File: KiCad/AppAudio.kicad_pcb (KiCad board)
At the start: 2 copper layers, 4.3 x 3.1 mm, 32 parts, among them P1 WRITER-VCC, Q1 Q_NMOS_SGD, SW1 SWITCH_INV, SW2 SW_PUSH, U1 TWE_LITE_SMD, U2 LMC6062, U3 HT82V739

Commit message: PCB design in progress.
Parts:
- added REF**: PCB-LC115H, favorites:PCB-LC115H, F.Cu at (100.0, 100.0)
- R10, R13, R4: footprint Resistors_ThroughHole:Resistor_Horizontal_RM10mm -> Resistors_SMD:R_0603_HandSoldering
- SW1: value SWITCH_INV -> SW_PUSH; footprint Terminal_Blocks:TerminalBlock_WAGO-236_2Stift_RM5mm_3pol -> favorites:JB-15HFBP2
- SW2: footprint favorites:JB-15HFBP2 -> favorites:DTS-6
- VR1, VR2: footprint favorites:RV-TSR-3386T -> favorites:RV-3362P
- moved R9 123.8 mm to (1.84, 133.5)
- moved P1 122.7 mm to (73.5, 94.0), turned to 270 degrees
- moved SP1 116.6 mm to (3.41, 162.3)
- moved C2 116.6 mm to (-22.8, 100.3)
- moved C4 116.6 mm to (-18.5, 102.1)
- moved C5 116.6 mm to (-31.3, 105.7)
- moved Q1 116.6 mm to (-7.20, 125.5)
- moved R11 116.6 mm to (37.4, 126.8)
- moved C7 116.6 mm to (-27.0, 107.4)
- moved R12 116.6 mm to (50.2, 125.0)
- moved R7 116.6 mm to (10.3, 149.2)
- moved R8 116.6 mm to (10.1, 143.2)
- moved R4 94.4 mm to (148.0, 92.5), turned to 0 degrees
- moved R13 91.8 mm to (87.0, 52.5)
- moved R10 87.8 mm to (50.0, 64.0)
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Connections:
- SW1 pad 1: GND -> Net-(SW1-Pad1)
- SW1 pad 2: Net-(SW1-Pad2) -> GND
- U1 pad 13: Net-(SW2-Pad1) -> Net-(SW1-Pad1)
- U1 pad 15: Net-(SW1-Pad2) -> Net-(SW2-Pad1)
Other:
- board size 4.3 x 3.1 mm -> 60 x 63 mm

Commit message: Fixed wires.
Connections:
- U1 pad 8: /RXD -> /TXD
- U1 pad 9: /TXD -> /RXD
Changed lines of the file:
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@@
     (links 67)
     (no_connects 67)
-    (area -32.687973 49.475 150.225001 181.591001)
+    (area 0 0 0 0)
     (thickness 1.6)
     (drawings 0)
@@
       (net 35 "Net-(U1-Pad7)"))
     (pad 8 smd oval (at -6.735 4.445 90) (size 0.9 1.4) (layers F.Cu F.Paste F.Mask)
+      (net 18 /TXD))
+    (pad 9 smd oval (at -4.445 6.735) (size 0.9 1.4) (layers F.Cu F.Paste F.Mask)
       (net 16 /RXD))
-    (pad 9 smd oval (at -4.445 6.735) (size 0.9 1.4) (layers F.Cu F.Paste F.Mask)
-      (net 18 /TXD))
     (pad 10 smd oval (at -3.175 6.735) (size 0.9 1.4) (layers F.Cu F.Paste F.Mask)
       (net 36 "Net-(U1-Pad10)"))

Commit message: PCB layout has done.
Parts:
- added BT1: Battery, Pin_Headers:Pin_Header_Straight_1x02, B.Cu at (110.5, 124.0)
- C1, C3, P1, Q1, R10, R13, R4, SP1, VR1, VR2: moved to B.Cu
- C6: footprint Capacitors_ThroughHole:C_Radial_D8_L11.5_P3.5 -> Capacitors_ThroughHole:C_Radial_D6.3_L11.2_P2.5; moved to B.Cu
- MIC1: footprint Capacitors_ThroughHole:C_Radial_D6.3_L11.2_P2.5 -> favorites:DB-C9767
- moved C5 151.9 mm to (118.0, 77.5), turned to 180 degrees
- moved C4 137.8 mm to (119.0, 94.0), turned to 270 degrees
- moved C2 137.4 mm to (114.5, 94.0), turned to 270 degrees
- moved R7 121.7 mm to (122.5, 102.0), turned to 270 degrees
- moved R8 114.5 mm to (117.0, 102.0), turned to 270 degrees
- moved C7 113.6 mm to (86.5, 111.5), turned to 180 degrees
- moved SP1 112.1 mm to (75.5, 76.5), turned to 180 degrees
- moved R9 104.9 mm to (100.3, 97.5)
- moved Q1 103.7 mm to (85.0, 78.0)
- moved R5 78.9 mm to (107.5, 102.0), turned to 270 degrees
- moved C3 77.6 mm to (113.5, 117.0)
- moved R6 72.4 mm to (77.5, 112.2)
- moved R3 70.6 mm to (123.5, 98.0)
- moved VR1 70.5 mm to (114.0, 71.5), turned to 180 degrees
- moved R2 64.1 mm to (112.5, 102.0), turned to 270 degrees
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
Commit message: Relocated.
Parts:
- moved C6 13.0 mm to (93.0, 112.0)
- moved R10 10.6 mm to (77.0, 88.0)
- moved Q1 10.4 mm to (82.0, 88.0)
- moved R13 10.4 mm to (86.5, 88.1)
- moved C1 5.15 mm to (72.0, 110.0), turned to 0 degrees
- moved VR2 2.51 mm to (77.0, 120.0)
- moved SP1 2.20 mm to (77.5, 77.5), turned to 270 degrees
- moved R6 0.50 mm to (78.0, 112.2)
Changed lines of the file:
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@@
   )
   (module Resistors_ThroughHole:Resistor_Horizontal_RM10mm (layer F.Cu)
-    (at 77.5 112.16 90)
+    (at 78 112.16 90)
     (descr "Resistor, Axial,  RM 10mm, 1/3W")
     (tags "Resistor Axial RM 10mm 1/3W")
@@
   )
   (module Capacitors_ThroughHole:C_Radial_D8_L11.5_P3.5 (layer B.Cu)
-    (at 74.5 105.5 270)
+    (at 72 110)
     (descr "Radial Electrolytic Capacitor Diameter 8mm x Length 11.5mm, Pitch 3.5mm")
     (tags "Electrolytic Capacitor")
-    (fp_text reference C1 (at 1.75 5.3 270) (layer B.SilkS)
-      (effects (font (size 1 1) (thickness 0.15)) (justify mirror))
-    )
-    (fp_text value 33u (at 1.75 -5.3 270) (layer B.Fab)
+    (fp_text reference C1 (at 1.75 5.3) (layer B.SilkS)
+      (effects (font (size 1 1) (thickness 0.15)) (justify mirror))
+    )
+    (fp_text value 33u (at 1.75 -5.3) (layer B.Fab)
       (effects (font (size 1 1) (thickness 0.15)) (justify mirror))
     )
@@
     (fp_circle (center 1.75 0) (end 1.75 4.0375) (layer B.SilkS) (width 0.15))
     (fp_circle (center 1.75 0) (end 1.75 4.3) (layer B.CrtYd) (width 0.05))
-    (pad 2 thru_hole circle (at 3.5 0 270) (size 1.3 1.3) (drill 0.8) (layers *.Cu *.Mask B.SilkS)
+    (pad 2 thru_hole circle (at 3.5 0) (size 1.3 1.3) (drill 0.8) (layers *.Cu *.Mask B.SilkS)
       (net 2 "Net-(C1-Pad2)"))
-    (pad 1 thru_hole rect (at 0 0 270) (size 1.3 1.3) (drill 0.8) (layers *.Cu *.Mask B.SilkS)
+    (pad 1 thru_hole rect (at 0 0) (size 1.3 1.3) (drill 0.8) (layers *.Cu *.Mask B.SilkS)
       (net 1 "Net-(C1-Pad1)"))
     (model Capacitors_ThroughHole.3dshapes/C_Radial_D8_L11.5_P3.5.wrl
@@
   )
   (module favorites:EMT3 (layer B.Cu)
-    (at 85 78)
+    (at 82 88)
     (descr EMT3)
     (attr smd)
-    (fp_text reference Q1 (at 0 -1.524) (layer B.SilkS)
-      (effects (font (size 0.29972 0.29972) (thickness 0.06096)) (justify mirror))
+    (fp_text reference Q1 (at 0 -2.5) (layer B.SilkS)
+      (effects (font (size 1 1) (thickness 0.1)) (justify mirror))
     )
     (fp_text value Q_NMOS_SGD (at 0 -0.3302) (layer B.SilkS) hide
@@
   )
   (module Pin_Headers:Pin_Header_Straight_1x02 (layer B.Cu)
-    (at 75.5 76.5 180)
+    (at 77.46 77.5 270)
     (descr "Through hole pin header")
     (tags "pin header")
-    (fp_text reference SP1 (at 0 5.1 180) (layer B.SilkS)
-      (effects (font (size 1 1) (thickness 0.15)) (justify mirror))
-    )
-    (fp_text value SPEAKER (at 0 3.1 180) (layer B.Fab)
+    (fp_text reference SP1 (at 0 2.46 270) (layer B.SilkS)
+      (effects (font (size 1 1) (thickness 0.15)) (justify mirror))
+    )
+    (fp_text value SPEAKER (at 0.5 -5.54 270) (layer B.Fab)
       (effects (font (size 1 1) (thickness 0.15)) (justify mirror))
     )
@@
     (fp_line (start -1.27 -1.27) (end -1.27 -3.81) (layer B.SilkS) (width 0.15))
     (fp_line (start -1.27 -3.81) (end 1.27 -3.81) (layer B.SilkS) (width 0.15))
-    (pad 1 thru_hole rect (at 0 0 180) (size 2.032 2.032) (drill 1.016) (layers *.Cu *.Mask B.SilkS)
+    (pad 1 thru_hole rect (at 0 0 270) (size 2.032 2.032) (drill 1.016) (layers *.Cu *.Mask B.SilkS)
       (net 27 "Net-(SP1-Pad1)"))
-    (pad 2 thru_hole oval (at 0 -2.54 180) (size 2.032 2.032) (drill 1.016) (layers *.Cu *.Mask B.SilkS)
+    (pad 2 thru_hole oval (at 0 -2.54 270) (size 2.032 2.032) (drill 1.016) (layers *.Cu *.Mask B.SilkS)
       (net 28 "Net-(SP1-Pad2)"))
     (model Pin_Headers.3dshapes/Pin_Header_Straight_1x02.wrl
@@
   (module favorites:PCB-LC115H (layer F.Cu)
     (at 96.5 98.5)
-    (fp_text reference REF** (at 0 26) (layer F.SilkS)
+    (fp_text reference REF** (at -0.5 -33.5) (layer F.SilkS)
       (effects (font (size 1 1) (thickness 0.15)))
     )
@@
       (effects (font (size 1 1) (thickness 0.15)))
     )
-    (fp_text value SW_PUSH (at 0 -6.6 90) (layer F.SilkS)
+    (fp_text value SW_PUSH (at 0 -6.6 90) (layer F.Fab)
       (effects (font (size 1 1) (thickness 0.15)))
     )
@@
   )
   (module Resistors_SMD:R_0603_HandSoldering (layer B.Cu)
-    (at 80.5 78 90)
+    (at 77 88 90)
     (descr "Resistor SMD 0603, hand soldering")
     (tags "resistor 0603")
@@
   )
   (module Resistors_SMD:R_0603_HandSoldering (layer B.Cu)
-    (at 89 78 90)
+    (at 86.5 88.1 90)
     (descr "Resistor SMD 0603, hand soldering")
     (tags "resistor 0603")
@@
   )
   (module favorites:RV-3362P (layer B.Cu)
-    (at 77.5 117.54)
+    (at 77 120)
     (fp_text reference VR2 (at 0 -4.43) (layer B.SilkS)
       (effects (font (size 1 1) (thickness 0.15)) (justify mirror))
@@
   )
   (module Capacitors_ThroughHole:C_Radial_D6.3_L11.2_P2.5 (layer B.Cu)
-    (at 93.5 99)
+    (at 93 112)
     (descr "Radial Electrolytic Capacitor, Diameter 6.3mm x Length 11.2mm, Pitch 2.5mm")
     (tags "Electrolytic Capacitor")

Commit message: Changed the footprint of the LED.
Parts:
- D1: footprint LEDs:LED-5MM-3 -> favorites:LED-SQ3MM-3
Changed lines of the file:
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@@
-    )
-  )
-  (module LEDs:LED-5MM-3 (layer F.Cu)
-    (at 79.96 70.5)
-    (descr "3-lead LED 5mm - Lead pitch 100mil (2,54mm)")
-    (tags "LED led 5mm 5MM 100mil 2.54mm 3-lead")
-    (fp_text reference D1 (at 2.54508 -3.91668) (layer F.SilkS)
-      (effects (font (size 1 1) (thickness 0.15)))
-    )
-    (fp_text value Led_x2 (at 2.58064 4.22148) (layer F.Fab)
-      (effects (font (size 1 1) (thickness 0.15)))
-    )
-    (fp_arc (start 0 0) (end -0.5 1) (angle 125) (layer F.CrtYd) (width 0.05))
-    (fp_arc (start 2.54 0) (end -0.5 -1.55) (angle 139) (layer F.CrtYd) (width 0.05))
-    (fp_arc (start 5.08 0) (end 5.85 -0.8) (angle 90) (layer F.CrtYd) (width 0.05))
-    (fp_arc (start 2.54 0) (end -0.5 1.55) (angle -139.8) (layer F.CrtYd) (width 0.05))
-    (fp_arc (start 2.54 0) (end -0.254 1.51) (angle -135) (layer F.SilkS) (width 0.15))
-    (fp_arc (start 2.54 0) (end -0.254 -1.51) (angle 135) (layer F.SilkS) (width 0.15))
-    (fp_line (start -0.5 -1) (end -0.5 -1.55) (layer F.CrtYd) (width 0.05))
-    (fp_line (start -0.5 1) (end -0.5 1.55) (layer F.CrtYd) (width 0.05))
-    (fp_arc (start 2.286 0) (end 3.429 -1.143) (angle -90) (layer F.SilkS) (width 0.15))
-    (fp_arc (start 2.286 0) (end 1.27 1.143) (angle -90) (layer F.SilkS) (width 0.15))
-    (fp_arc (start 2.286 0) (end 0.381 1.016) (angle -90) (layer F.SilkS) (width 0.15))
-    (fp_arc (start 2.286 0) (end 1.524 2.032) (angle -90) (layer F.SilkS) (width 0.15))
-    (fp_arc (start 2.286 0) (end 4.318 -0.762) (angle -90) (layer F.SilkS) (width 0.15))
-    (fp_arc (start 2.286 0) (end 3.302 -1.905) (angle -90) (layer F.SilkS) (width 0.15))
-    (fp_arc (start 2.286 0) (end 0.762 1.524) (angle -90) (layer F.SilkS) (width 0.15))
-    (fp_arc (start 2.286 0) (end 3.81 -1.524) (angle -90) (layer F.SilkS) (width 0.15))
-    (fp_line (start -0.254 1) (end -0.254 1.51) (layer F.SilkS) (width 0.15))
-    (fp_line (start -0.254 -1.51) (end -0.254 -1) (layer F.SilkS) (width 0.15))
-    (pad 1 thru_hole circle (at 0 0 180) (size 1.6764 1.6764) (drill 0.8128) (layers *.Cu *.Mask F.SilkS)
-      (net 11 "Net-(D1-Pad1)"))
-    (pad 2 thru_hole circle (at 2.54 0 180) (size 1.6764 1.6764) (drill 0.8128) (layers *.Cu *.Mask F.SilkS)
-      (net 12 "Net-(D1-Pad2)"))
-    (pad 3 thru_hole circle (at 5.08 0 180) (size 1.6764 1.6764) (drill 0.8128) (layers *.Cu *.Mask F.SilkS)
-      (net 13 "Net-(D1-Pad3)"))
-    (model LEDs.3dshapes/LED-5MM-3.wrl
-      (at (xyz 0.1 0 0))
-      (scale (xyz 4 4 4))
-      (rotate (xyz 0 0 180))
     )
   )
@@
       (rotate (xyz 0 0 0))
     )
+  )
+  (module favorites:LED-SQ3MM-3 (layer F.Cu)
+    (at 79.96 70.5)
+    (fp_text reference D1 (at 0 2.54) (layer F.SilkS)
+      (effects (font (size 1 1) (thickness 0.15)))
+    )
+    (fp_text value Led_x2 (at 0 -2.54) (layer F.Fab)
+      (effects (font (size 1 1) (thickness 0.15)))
+    )
+    (fp_text user 1 (at -3.3 1.3) (layer F.SilkS)
+      (effects (font (size 1 1) (thickness 0.15)))
+    )
+    (fp_line (start -2.2 -0.9) (end -2.2 -1.6) (layer F.SilkS) (width 0.15))
+    (fp_line (start 2.1 0.9) (end 2.1 1.6) (layer F.SilkS) (width 0.15))
+    (fp_line (start 2.1 1.6) (end -2.2 1.6) (layer F.SilkS) (width 0.15))
+    (fp_line (start -2.2 1.6) (end -2.2 0.9) (layer F.SilkS) (width 0.15))
+    (fp_line (start -2.2 -1.6) (end 2.2 -1.6) (layer F.SilkS) (width 0.15))
+    (fp_line (start 2.2 -1.6) (end 2.2 -0.9) (layer F.SilkS) (width 0.15))
+    (pad 1 thru_hole circle (at -2.54 0) (size 1.524 1.524) (drill 0.762) (layers *.Cu *.Mask F.SilkS)
+      (net 11 "Net-(D1-Pad1)"))
+    (pad 2 thru_hole circle (at 0 0) (size 1.524 1.524) (drill 0.762) (layers *.Cu *.Mask F.SilkS)
+      (net 12 "Net-(D1-Pad2)"))
+    (pad 3 thru_hole circle (at 2.54 0) (size 1.524 1.524) (drill 0.762) (layers *.Cu *.Mask F.SilkS)
+      (net 13 "Net-(D1-Pad3)"))
+    (model favorites.3dshapes/GL8ED48.wrl
+      (at (xyz 0 0 -0.118))
+      (scale (xyz 0.393701 0.393701 0.393701))
+      (rotate (xyz 0 0 0))
+    )

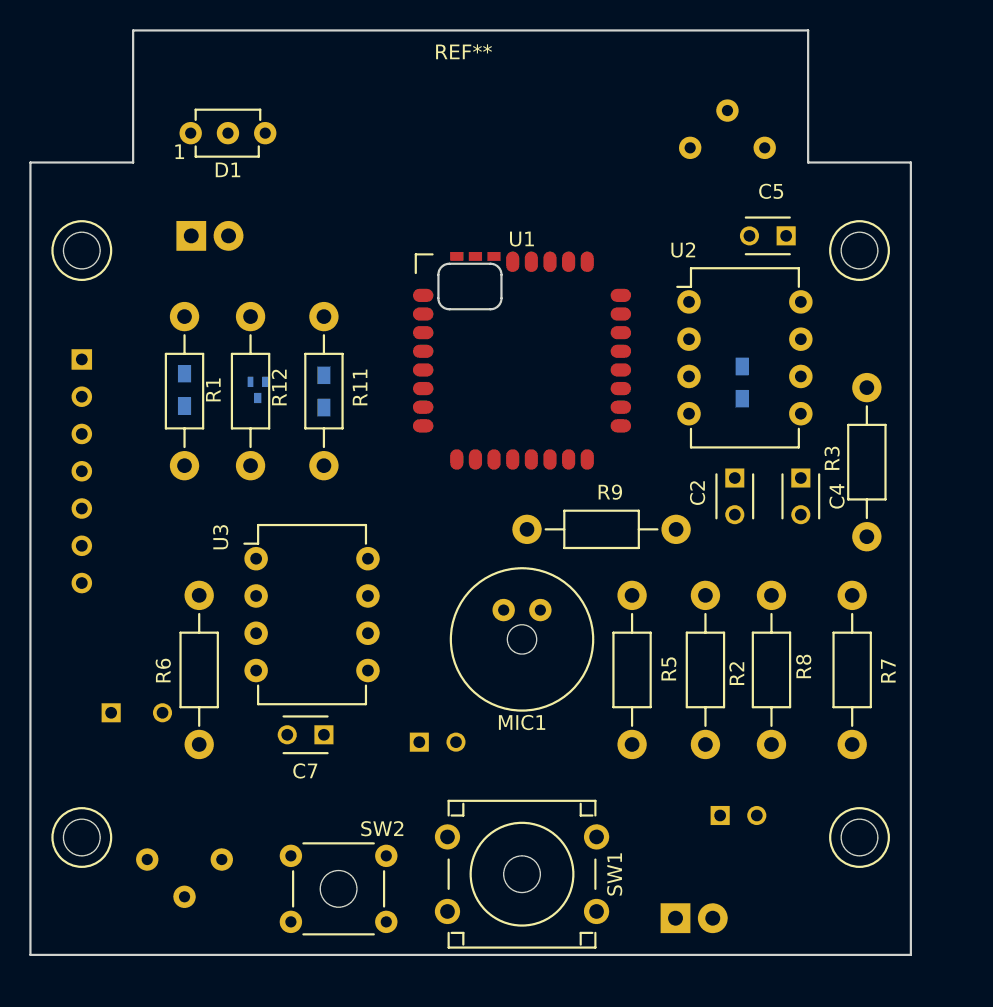
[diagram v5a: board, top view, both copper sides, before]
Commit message: Added the 3d model of the speaker.
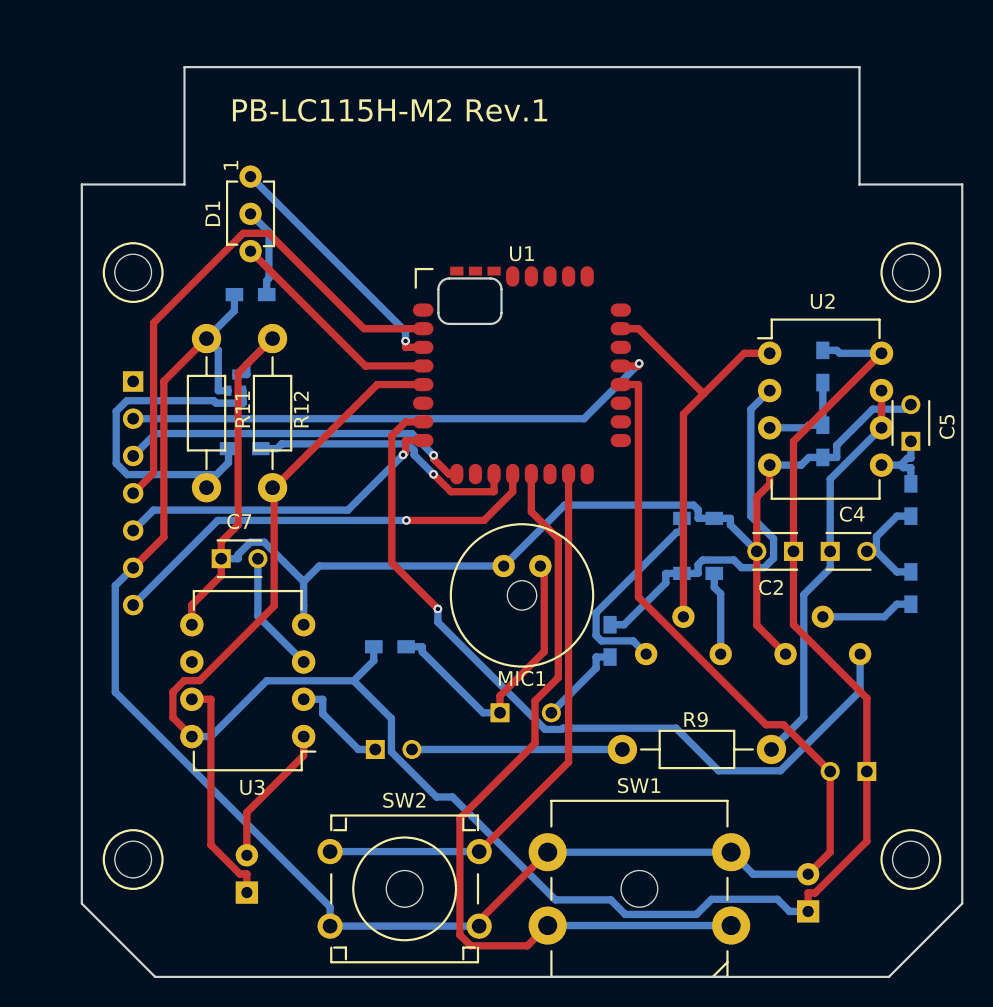
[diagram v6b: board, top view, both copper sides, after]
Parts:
- BT1, SP1: footprint Pin_Headers:Pin_Header_Straight_1x02 -> favorites:B02B-XASK-1
- PB1: renamed from REF**; value PCB-LC115H -> PB-LC115H-M2
- R1, R2, R3, R5, R6, R7, R8: footprint Resistors_ThroughHole:Resistor_Horizontal_RM10mm -> Resistors_SMD:R_0603_HandSoldering; moved to B.Cu
- SW1: footprint favorites:JB-15HFBP2 -> favorites:TVGP01-G73BB
- SW2: footprint favorites:DTS-6 -> favorites:JB-15HFBP2
- moved VR2 45.7 mm to (120.5, 106.0), turned to 180 degrees
- moved SP1 44.9 mm to (81.2, 122.2), turned to 0 degrees
- moved R6 37.3 mm to (112.0, 96.8), turned to 180 degrees
- moved VR1 34.6 mm to (111.0, 106.0)
- moved C1 26.5 mm to (98.5, 110.0)
- moved R1 18.7 mm to (91.0, 105.5), turned to 0 degrees
- moved C5 16.4 mm to (126.5, 91.5), turned to 90 degrees
- moved R9 16.3 mm to (106.8, 112.5)
- moved C7 13.9 mm to (79.5, 99.5), turned to 0 degrees
- moved U3 12.5 mm to (85.1, 111.6), turned to 180 degrees
- moved R3 12.0 mm to (120.5, 86.4), turned to 270 degrees
- moved R8 11.5 mm to (126.5, 95.5)
- moved C3 10.4 mm to (123.5, 114.0), turned to 180 degrees
- moved BT1 9.05 mm to (119.5, 123.5), turned to 0 degrees
- moved R13 8.28 mm to (81.5, 81.5), turned to 180 degrees
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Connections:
- net Net-(C6-Pad1) renamed /Aud_In
- net Net-(C7-Pad2) renamed /VREF
- SP1 pad 1: Net-(SP1-Pad1) -> /OUTP
- SP1 pad 2: Net-(SP1-Pad2) -> /OUTN
- U3 pad 1: Net-(SP1-Pad1) -> /OUTN
- U3 pad 7: Net-(SP1-Pad2) -> /OUTP
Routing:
- net VCC: track 0.00 -> 137.9 mm
- net GND: track 0.00 -> 133.8 mm
- net VSS: track 0.00 -> 96.8 mm
- net Net-(U1-Pad7): track 0.00 -> 54.3 mm, vias 0 -> 1
- net Net-(SW1-Pad1): track 0.00 -> 54.3 mm
- net Net-(SW2-Pad1): track 0.00 -> 38.4 mm
- net /RST: track 0.00 -> 37.4 mm, vias 0 -> 1
- net /PRG: track 0.00 -> 35.8 mm
- net /CFG: track 0.00 -> 30.3 mm, vias 0 -> 1
- net Net-(U1-Pad23): track 0.00 -> 28.9 mm
- net Net-(C4-Pad1): track 0.00 -> 27.6 mm
- net Net-(R2-Pad1): track 0.00 -> 26.8 mm
- net /RXD: track 0.00 -> 24.0 mm, vias 0 -> 1
- net Net-(Q1-Pad2): track 0.00 -> 23.6 mm
- net /TXD: track 0.00 -> 22.8 mm, vias 0 -> 1
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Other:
- board size 60 x 63 mm -> 60 x 62 mm
- net class Default: trace_width 0.25 -> 0.5
- board text added: "PB-LC115H-M2 Rev.1"
